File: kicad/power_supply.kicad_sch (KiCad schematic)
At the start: 33 parts, among them Q1 CSD19537Q3, Q2 BSS138, U1 TPS26632RGE, U2 LMR33610ADDAR, U3 LMR33610ADDAR

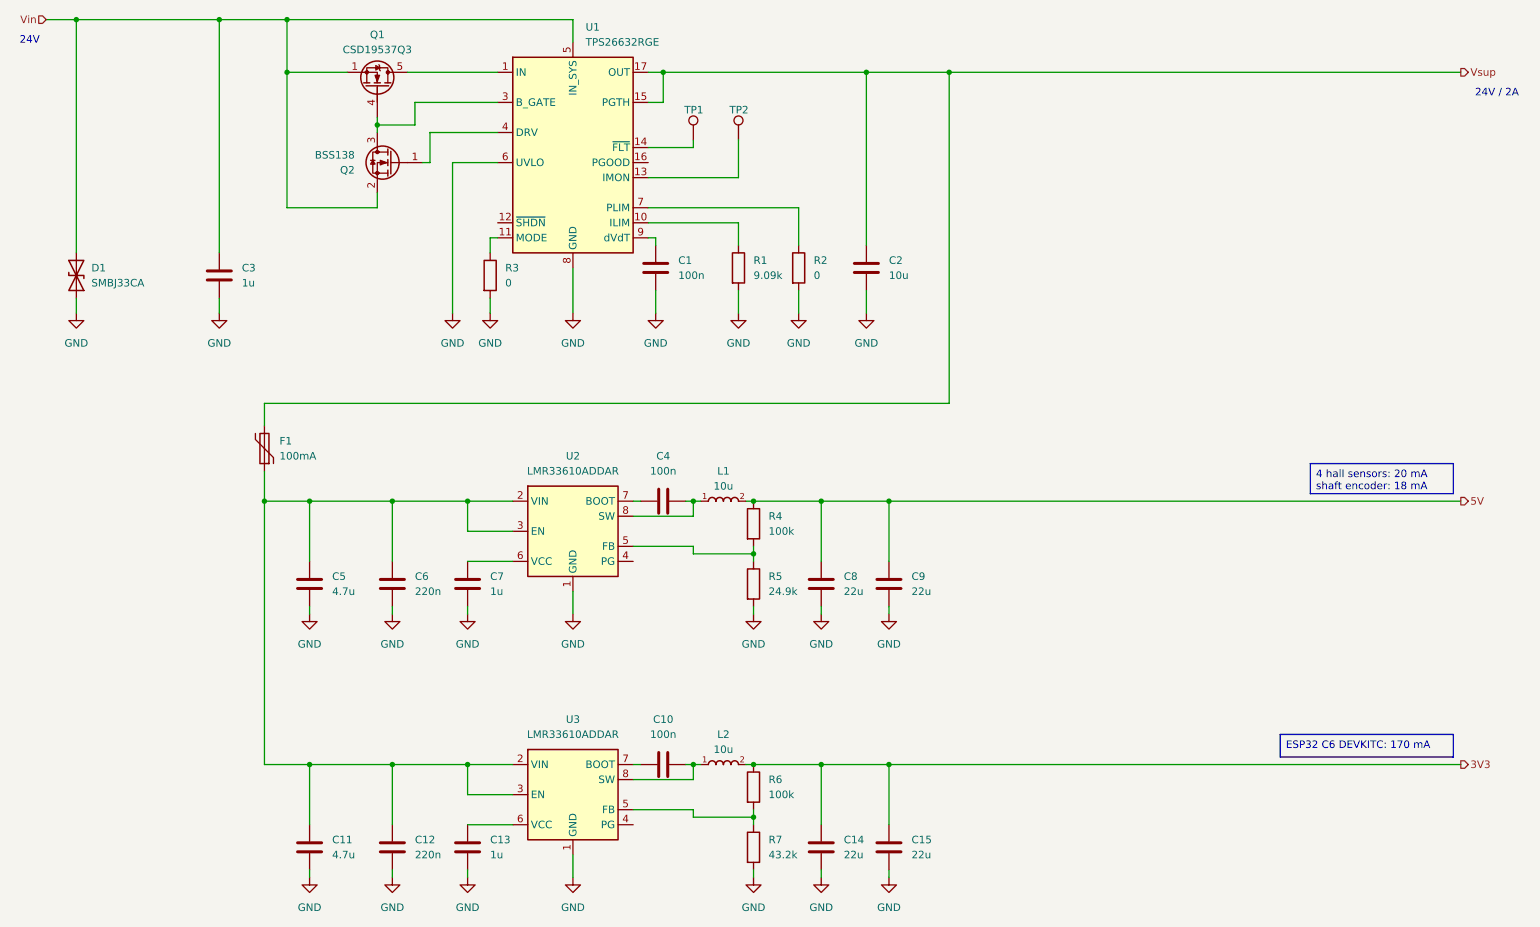
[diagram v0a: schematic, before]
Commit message: Fixed up or explained all DRC violations.
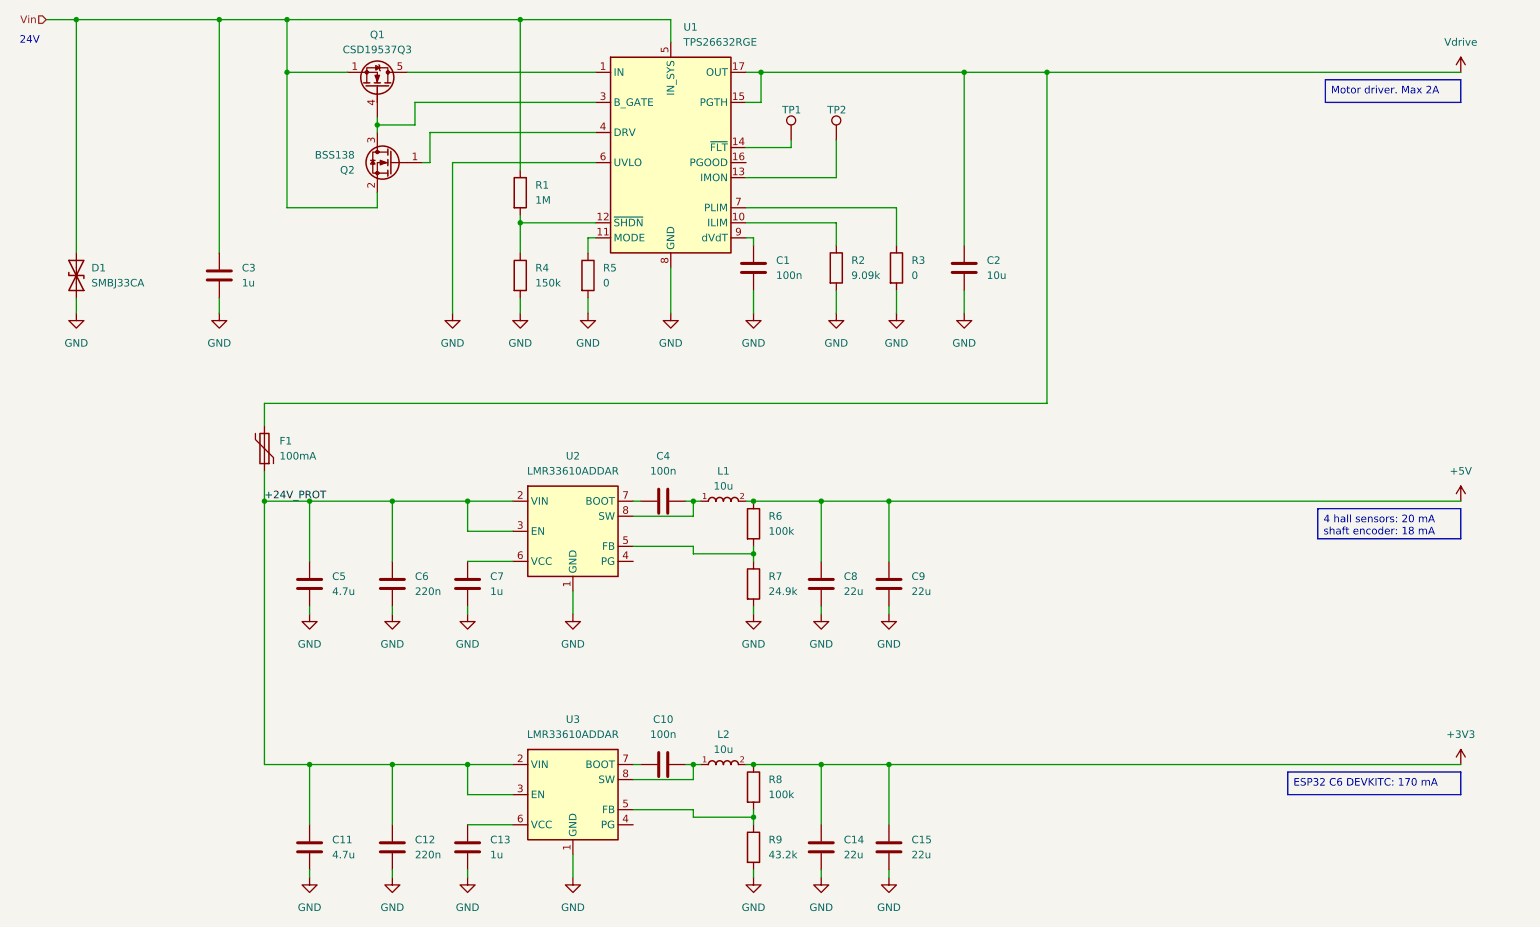
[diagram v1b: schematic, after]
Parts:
- added R1: 1M, Resistor_SMD:R_0603_1608Metric, symbol Device:R
- added R4: 150k, Resistor_SMD:R_0603_1608Metric, symbol Device:R
- renumbered R1 to R2, R2 to R3, R3 to R5, R4 to R6, R5 to R7, R6 to R8, R7 to R9
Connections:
- net GND: now also R4.2
- net Vin: now also R1.1
- net +24V_PROT: now reaches C11.1, C12.1, C5.1, C6.1, F1.1, U2.2 (VIN), U2.3 (EN), U3.2 (VIN), U3.3 (EN)
- net at U1.12 (~{SHDN}): now also R1.2, R4.1
- net 3V3 renamed +3V3
- net 5V renamed +5V
- net Vsup renamed Vdrive
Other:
- note removed: "24V / 2A"
- moved on the sheet: C1, C2, R2, R3, R5, TP1, TP2, U1

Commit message: Supplying the ESP32-C6-DEVKIT with 5V and using its 3V3 output to supply the boards logic. Removed the 3V3 switch mode power supply on the board.
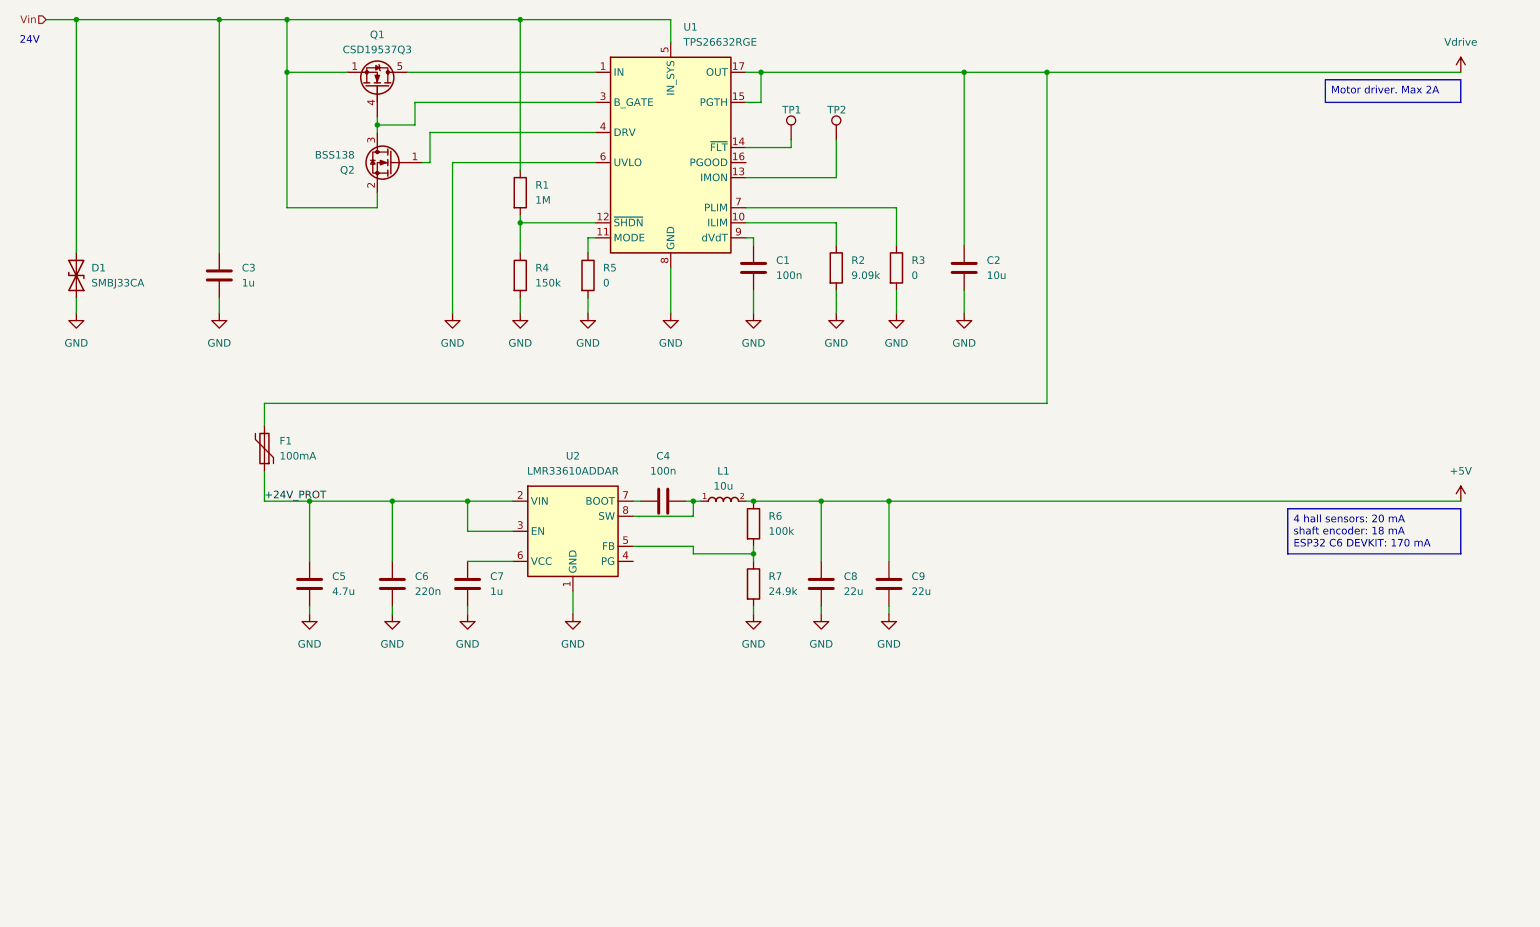
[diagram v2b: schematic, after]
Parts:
- removed C10: 100n, Capacitor_SMD:C_0603_1608Metric, symbol Device:C
- removed C11: 4.7u, Capacitor_SMD:C_0805_2012Metric, symbol Device:C
- removed C12: 220n, Capacitor_SMD:C_0603_1608Metric, symbol Device:C
- removed C13: 1u, Capacitor_SMD:C_0603_1608Metric, symbol Device:C
- removed C14, C15: 22u, Capacitor_SMD:C_1206_3216Metric, symbol Device:C
- removed L2: 10u, local_library:IND_SRP4020TA-100M, symbol local_library:SRP4020TA-100M
- removed R8: 100k, Resistor_SMD:R_0603_1608Metric, symbol Device:R
- removed R9: 43.2k, Resistor_SMD:R_0603_1608Metric, symbol Device:R
- removed U3: LMR33610ADDAR, local_library:Texas_HSOP-8-1EP_3.9x4.9mm_P1.27mm_ThermalVias, symbol Regulator_Switching:LMR33610ADDAR

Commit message: Added extra copper for cooling the DRV8452SPWPR motor driver.
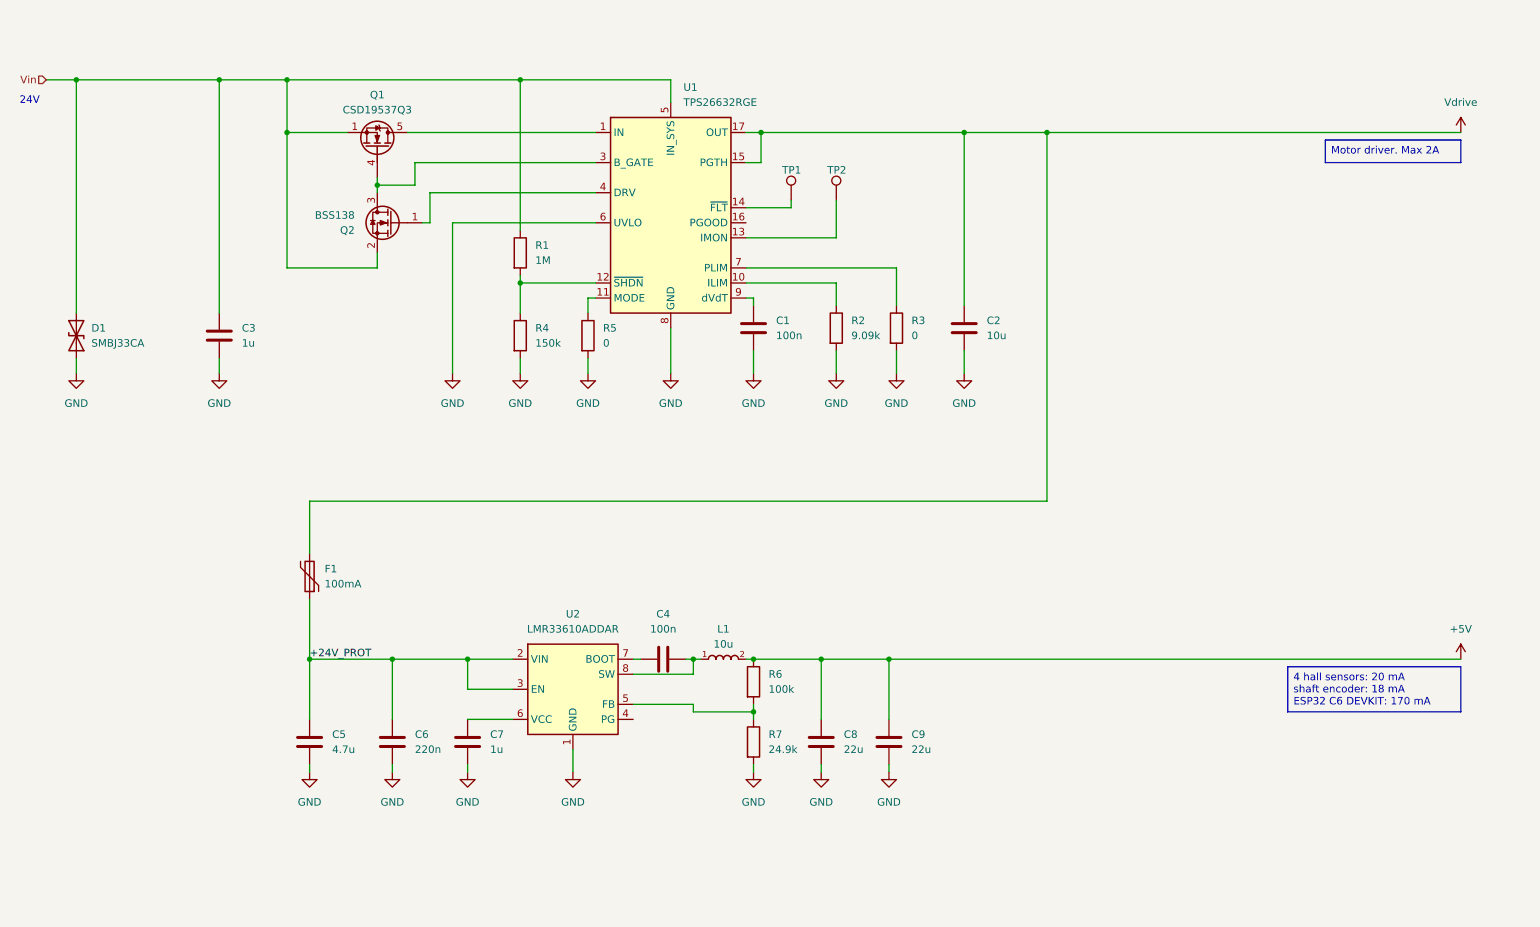
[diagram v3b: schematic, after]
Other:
- moved on the sheet: C1, C2, C3, C4, C5, C6, C7, C8, C9, D1, F1, L1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

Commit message: Updated to use more of JCLPCB's basic components. Added extra field "FT Rotation Offset" to get the correct orientation for placement at JCLPCB.
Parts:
- C1, C4: Dielectric X7R -> (none); LCSC (none) -> C14663; MF Murata -> Yageo; MP GRM188R72A104KA35D -> CC0603KRX7R9BB104; SupplierPN 490-3285-1-ND -> 311-1344-1-ND; Voltage 100V -> 50V
- C2: Dielectric X5R -> (none); LCSC (none) -> C440198
- C3, C7: Dielectric X7T -> (none); LCSC (none) -> C15849; MF Murata -> Samsung; MP GRM188D71H105KE01J -> CL10A105KB8NNNC; SupplierPN 490-GRM188D71H105KE01JCT-ND -> 1276-1860-1-ND
- C5: Dielectric X5R -> (none); LCSC (none) -> C162420
- C6: Dielectric X7R -> (none); LCSC (none) -> C64705; MF Murata -> Samsung; MP GRM188R71H224KAC4J -> CL10B224KB8NNNC; SupplierPN 490-GRM188R71H224KAC4JCT-ND -> 1276-CL10B224KB8NNNCCT-ND
- C8, C9: Dielectric X7S -> (none); LCSC (none) -> C12891; MF Murata -> Samsung; MP GRM31CC71C226ME11L -> CL31A226KAHNNNE; SupplierPN 490-17691-1-ND -> 1276-3047-1-ND; Voltage 16V -> 25V
- D1: LCSC (none) -> C19077587; MF Bourns -> Hong Jiacheng; SupplierPN SMBJ33CABCT-ND -> SMBJ33CALFCT-ND
- F1: LCSC (none) -> C12430; Voltage 60V -> (none)
- L1: LCSC (none) -> C2847473
- Q1: value CSD19537Q3 -> BUK9M34-100EX; footprint Package_SON:VSON-8_3.3x3.3mm_P0.65mm_NexFET -> Package_TO_SOT_SMD:LFPAK33; symbol Transistor_FET:CSD19537Q3 -> Transistor_FET:BUK9M34-100EX; FT Rotation Offset (none) -> 270; LCSC (none) -> C550016; MF Texas Instruments -> Nexperia; MP CSD19537Q3 -> BUK9M34-100EX; SupplierPN 296-44351-1-ND -> 1727-2579-1-ND
- Q2: LCSC (none) -> C7420339; MF onsemi -> Hong Jiacheng; MP BSS138-G -> BSS138
- R1: LCSC (none) -> C22935; MF Yageo -> Uni Royal; MP RC0603FR-101ML -> 0603WAF1004T5E
- R2: value 9.09k -> 9.1k; LCSC (none) -> C23260; MF Yageo -> Uni Royal; MP RC0603FR-079K09L -> 0603WAF9101T5E; SupplierPN 311-9.09KHRCT-ND -> 311-9.10KHRCT-ND
- R3, R5: LCSC (none) -> C21189; MF Yageo -> Uni Royal; MP RC0603FR-100RL -> 0603WAF0000T5E
- R4: LCSC (none) -> C22807; MF Yageo -> Uni Royal; MP RC0603FR-07150KL -> 0603WAF1503T5E
- R6: LCSC (none) -> C25803; MF Yageo -> Uni Royal; MP RC0603FR-07100KL -> 0603WAF1003T5E
- R7: LCSC (none) -> C25962; MF Yageo -> Uni Royal; MP RC0603FR-0724K9L -> 0603WAF2492T5E
- TP1, TP2: now left out of the parts list
- U1: LCSC (none) -> C2862529
- U2: FT Rotation Offset (none) -> 90; LCSC (none) -> C1852147

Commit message: Fixed rotation for JLCPCB.
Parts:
- U2: FT Rotation Offset 90 -> 270
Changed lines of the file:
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@@
 			)
 		)
-		(property "FT Rotation Offset" "90"
+		(property "FT Rotation Offset" "270"
 			(at 115.57 129.54 0)
 			(effects
